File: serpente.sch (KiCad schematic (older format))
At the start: 24 parts, among them J1 USB_C_Receptacle_USB2.0, J2 Conn_Power, J3 Conn_GPIO, SW1 SW_RESET, U1 AT25SF081-XMHD-X, U2 MCP1700-3302E_SOT23, U3 ATSAMD21E1xA

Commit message: Rev 1
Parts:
- removed U1: AT25SF081-XMHD-X, Package_SO:TSSOP-8_4.4x3mm_P0.65mm, symbol Memory_Flash:AT25SF081-XMHD-X
- added R7, R8: 22R, Resistor_SMD:R_0603_1608Metric, symbol Device:R_Small
- added TP5: TP_USB_D-, TestPoint:TestPoint_Pad_D1.0mm, symbol Connector:TestPoint
- added TP6: TP_USB_D+, TestPoint:TestPoint_Pad_D1.0mm, symbol Connector:TestPoint
- added U1: GD25Q32CNIGR, Package_SON_Extra:USON-8_3x4mm_P0.8mm, symbol Memory_Flash_Extra:GD25Q32C
- C1, C2, C3, C4: footprint (none) -> Capacitor_SMD:C_0603_1608Metric
- D1, D2: footprint (none) -> Diode_SMD:D_SOD-323_HandSoldering
- D3: footprint (none) -> LED_SMD:LED_Cree-PLCC4_2x2mm_CW; symbol Device:LED_ARGB -> Device_Extra:LED_RBGA
- J1: footprint (none) -> Connector_USB_Extra:USB_C_Receptacle_GT-USB-7010
- J2: footprint (none) -> Connector_PinHeader_2.54mm:PinHeader_1x04_P2.54mm_Vertical
- J3: footprint (none) -> Connector_PinHeader_2.54mm:PinHeader_1x06_P2.54mm_Vertical
- R1: value TBD -> 360R; footprint (none) -> Resistor_SMD:R_0603_1608Metric
- R2, R3: value TBD -> 150R; footprint (none) -> Resistor_SMD:R_0603_1608Metric
- R4, R5, R6: footprint (none) -> Resistor_SMD:R_0603_1608Metric
- SW1: footprint (none) -> Button_Switch_SMD:SW_SPST_B3U-1000P
- TP1, TP2, TP3, TP4: footprint (none) -> TestPoint:TestPoint_Pad_D1.0mm
- U3: value ATSAMD21E1xA -> ATSAMD21E18A; footprint (none) -> Package_DFN_QFN:QFN-32-1EP_5x5mm_P0.5mm_EP3.6x3.6mm
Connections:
- wire segments 116 -> 120
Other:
- note added: "SERCOM 3 is always SPI FLASH\n\nPossible configs:\nSERCOM 0: SPI\n D0 - GPIO\n D1 - GPIO\n D2 - CS\n D3 - MISO\n D4 - SCK\n D5 - MOSI\n \nSERCOM 2: I2C\n D0 - SCL\n D1 - SDA\n D2 - GPIO\n D3 - GPIO\n D4 - GPIO\n D5 - GPIO\n\nSERCOM 0 or 2: UART\n D0 or D4 - RX\n D1 or D5 - TX\n D2 - GPIO\n D3 - GPIO\n\nSERCOM 0: UART, SERCOM 2: UART (2x UART)\n D0 - RX2\n D1 - TX2\n D2 - GPIO\n D3 - GPIO\n D4 - R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"
- note removed: "SERCOM 3 is always SPI FLASH\n\nPossible configs:\nSERCOM 0: SPI\n PA4 - MOSI\n PA5 - SCK\n PA6 - MISO\n PA7 - CS\n PA8 - GPIO\n PA9 - GPIO\n \nSERCOM 2: I2C\n PA4 - GPIO\n PA5 - GPIO\n PA6 - GPIO\n PA7 - GPIO\n PA8 - SDA\n PA9 - SCL\n\nSERCOM 0 or 2: UART\n PA4 or PA8 - TX\n PA6 - GPIO\n PA7 - GPIO\n PA5 or PA9 - RX\n\nSERCOM 0: UART, SERCOM 2: UART (2x UART)\n PA4 - TX0\n PA5 - RX0\n PA6 - GPIO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"
- note removed: "TODO:\nUpdate LED symbol\nUpdate FLASH symbol\nReplace PAx with GPIOx"
- moved on the sheet: J2, J3, R1, R2, R3, TP3, TP4

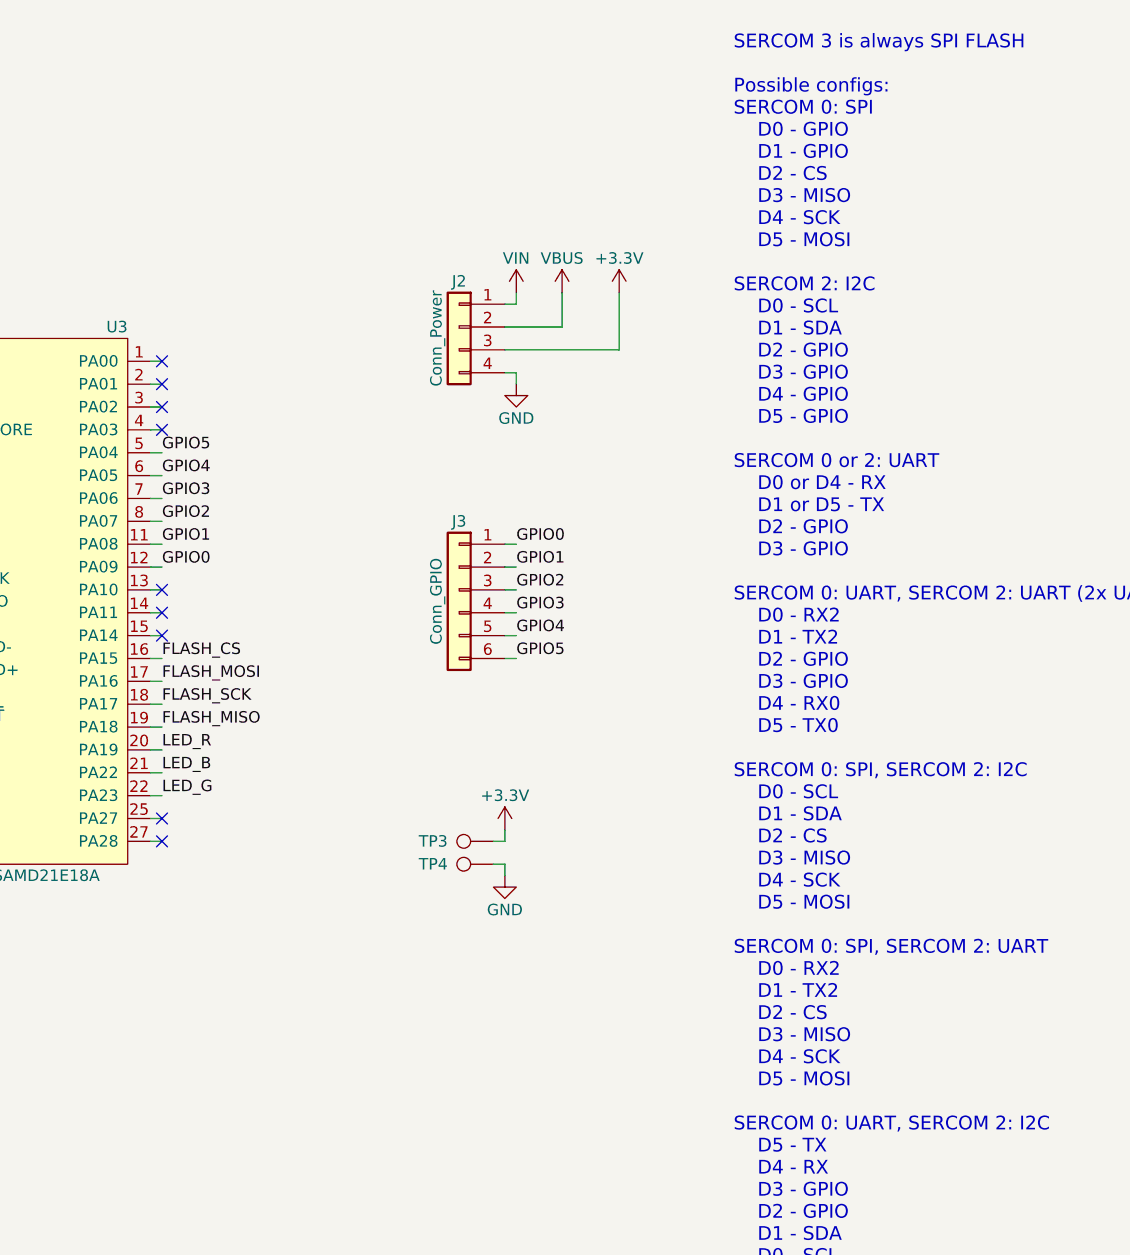
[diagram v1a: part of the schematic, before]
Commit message: Fix GPIO numbers, add BOM, update README
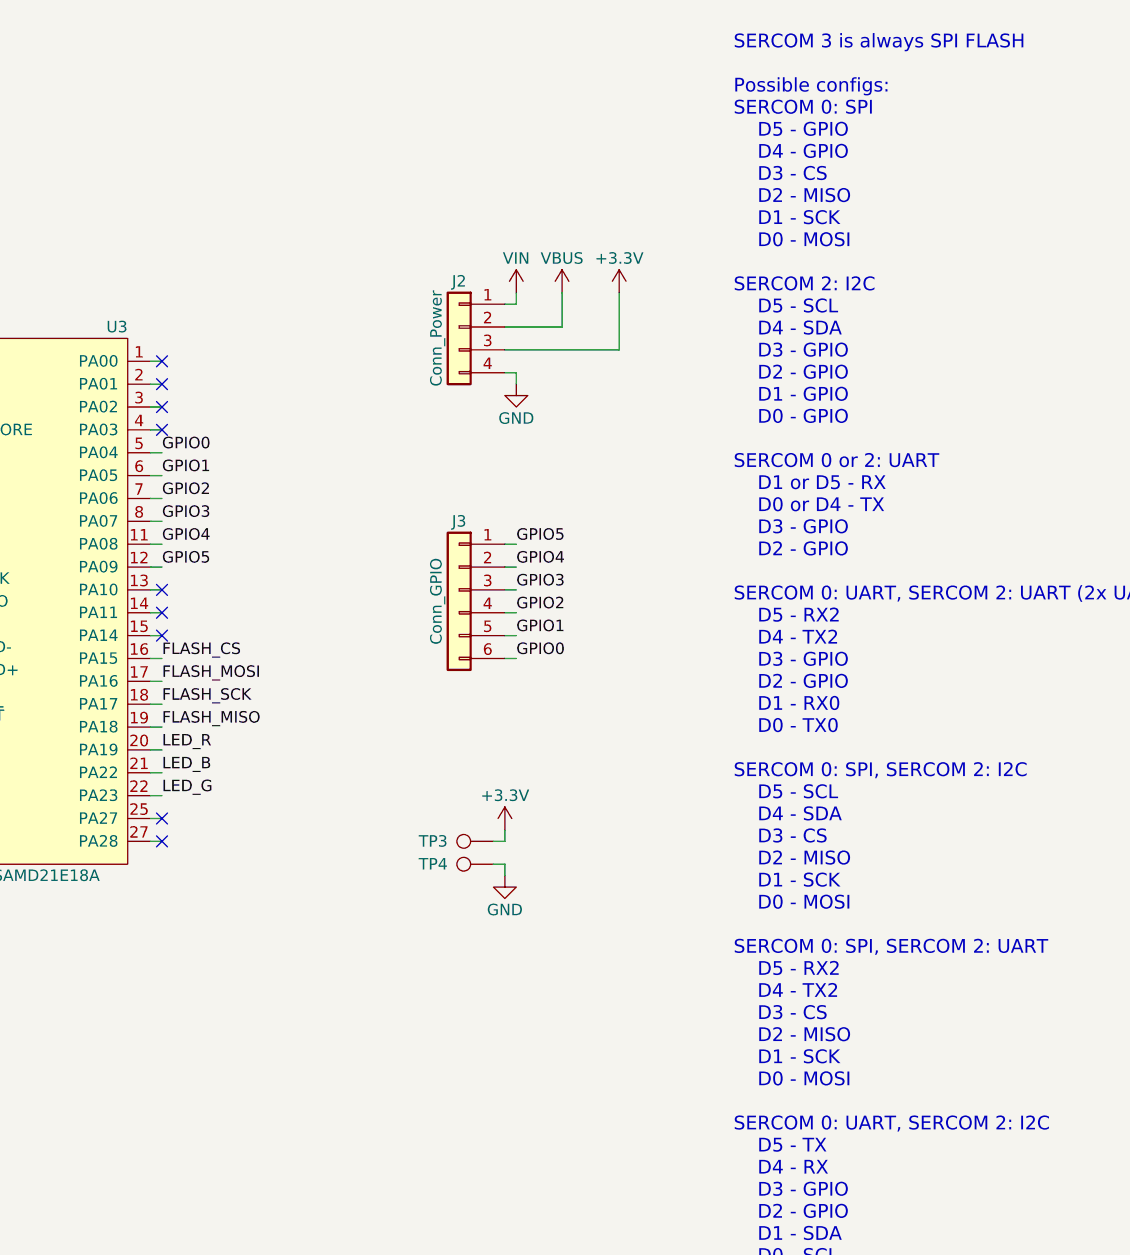
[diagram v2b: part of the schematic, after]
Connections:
- net GPIO0: now also J3.6 (Pin_6), U3.5 (PA04); no longer J3.1 (Pin_1), U3.12 (PA09)
- net GPIO1: now also J3.5 (Pin_5), U3.6 (PA05); no longer J3.2 (Pin_2), U3.11 (PA08)
- net GPIO2: now also J3.4 (Pin_4), U3.7 (PA06); no longer J3.3 (Pin_3), U3.8 (PA07)
- net GPIO3: now also J3.3 (Pin_3), U3.8 (PA07); no longer J3.4 (Pin_4), U3.7 (PA06)
- net GPIO4: now also J3.2 (Pin_2), U3.11 (PA08); no longer J3.5 (Pin_5), U3.6 (PA05)
- net GPIO5: now also J3.1 (Pin_1), U3.12 (PA09); no longer J3.6 (Pin_6), U3.5 (PA04)
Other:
- note added: "SERCOM 3 is always SPI FLASH\n\nPossible configs:\nSERCOM 0: SPI\n D5 - GPIO\n D4 - GPIO\n D3 - CS\n D2 - MISO\n D1 - SCK\n D0 - MOSI\n \nSERCOM 2: I2C\n D5 - SCL\n D4 - SDA\n D3 - GPIO\n D2 - GPIO\n D1 - GPIO\n D0 - GPIO\n\nSERCOM 0 or 2: UART\n D1 or D5 - RX\n D0 or D4 - TX\n D3 - GPIO\n D2 - GPIO\n\nSERCOM 0: UART, SERCOM 2: UART (2x UART)\n D5 - RX2\n D4 - TX2\n D3 - GPIO\n D2 - GPIO\n D1 - R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"
- note removed: "SERCOM 3 is always SPI FLASH\n\nPossible configs:\nSERCOM 0: SPI\n D0 - GPIO\n D1 - GPIO\n D2 - CS\n D3 - MISO\n D4 - SCK\n D5 - MOSI\n \nSERCOM 2: I2C\n D0 - SCL\n D1 - SDA\n D2 - GPIO\n D3 - GPIO\n D4 - GPIO\n D5 - GPIO\n\nSERCOM 0 or 2: UART\n D0 or D4 - RX\n D1 or D5 - TX\n D2 - GPIO\n D3 - GPIO\n\nSERCOM 0: UART, SERCOM 2: UART (2x UART)\n D0 - RX2\n D1 - TX2\n D2 - GPIO\n D3 - GPIO\n D4 - R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"
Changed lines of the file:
@@
 Text Label 6350 3900 0    50   ~ 0
 LED_B
+Text Label 7900 3400 0    50   ~ 0
+GPIO0
+Text Label 7900 3300 0    50   ~ 0
+GPIO1
+Text Label 7900 3200 0    50   ~ 0
+GPIO2
+Text Label 7900 3100 0    50   ~ 0
+GPIO3
+Text Label 7900 3000 0    50   ~ 0
+GPIO4
 Text Label 7900 2900 0    50   ~ 0
+GPIO5
+Text Label 6350 2500 0    50   ~ 0
 GPIO0
-Text Label 7900 3000 0    50   ~ 0
+Text Label 6350 2600 0    50   ~ 0
 GPIO1
-Text Label 7900 3100 0    50   ~ 0
+Text Label 6350 2700 0    50   ~ 0
 GPIO2
-Text Label 7900 3200 0    50   ~ 0
+Text Label 6350 2800 0    50   ~ 0
 GPIO3
-Text Label 7900 3300 0    50   ~ 0
+Text Label 6350 2900 0    50   ~ 0
 GPIO4
-Text Label 7900 3400 0    50   ~ 0
-GPIO5
 Text Label 6350 3000 0    50   ~ 0
-GPIO0
-Text Label 6350 2900 0    50   ~ 0
-GPIO1
-Text Label 6350 2800 0    50   ~ 0
-GPIO2
-Text Label 6350 2700 0    50   ~ 0
-GPIO3
-Text Label 6350 2600 0    50   ~ 0
-GPIO4
-Text Label 6350 2500 0    50   ~ 0
 GPIO5
 $Comp
@@
 FLASH_MISO
 Text Notes 8850 6250 0    60   ~ 0
-SERCOM 3 is always SPI FLASH\n\nPossible configs:\nSERCOM 0: SPI\n    D0 - GPIO\n    D1 - GPIO\n    D2 - CS\n    D3 - MISO\n    D4 - SCK\n    D5 - MOSI\n    \nSERCOM 2: I2C\n    D0 - SCL\n    D1 - SDA\n    D2 - GPIO\n    D3 - GPIO\n    D4 - GPIO\n    D5 - GPIO\n\nSERCOM 0 or 2: UART\n    D0 or D4 - RX\n    D1 or D5 - TX\n    D2 - GPIO\n    D3 - GPIO\n\nSERCOM 0: UART, SERCOM 2: UART (2x UART)\n    D0 - RX2\n    D1 - TX2\n    D2 - GPIO\n    D3 - GPIO\n    D4 - RX0\n    D5 - TX0\n\nSERCOM 0: SPI, SERCOM 2: I2C\n    D0 - SCL\n    D1 - SDA\n    D2 - CS\n    D3 - MISO\n    D4 - SCK\n    D5 - MOSI\n\nSERCOM 0: SPI, SERCOM 2: UART\n    D0 - RX2\n    D1 - TX2\n    D2 - CS\n    D3 - MISO\n    D4 - SCK\n    D5 - MOSI\n\nSERCOM 0: UART, SERCOM 2: I2C\n    D5 - TX\n    D4 - RX\n    D3 - GPIO\n    D2 - GPIO\n    D1 - SDA\n    D0 - SCL\n\nAll GPIOs are PWM-enabled!\n
+SERCOM 3 is always SPI FLASH\n\nPossible configs:\nSERCOM 0: SPI\n    D5 - GPIO\n    D4 - GPIO\n    D3 - CS\n    D2 - MISO\n    D1 - SCK\n    D0 - MOSI\n    \nSERCOM 2: I2C\n    D5 - SCL\n    D4 - SDA\n    D3 - GPIO\n    D2 - GPIO\n    D1 - GPIO\n    D0 - GPIO\n\nSERCOM 0 or 2: UART\n    D1 or D5 - RX\n    D0 or D4 - TX\n    D3 - GPIO\n    D2 - GPIO\n\nSERCOM 0: UART, SERCOM 2: UART (2x UART)\n    D5 - RX2\n    D4 - TX2\n    D3 - GPIO\n    D2 - GPIO\n    D1 - RX0\n    D0 - TX0\n\nSERCOM 0: SPI, SERCOM 2: I2C\n    D5 - SCL\n    D4 - SDA\n    D3 - CS\n    D2 - MISO\n    D1 - SCK\n    D0 - MOSI\n\nSERCOM 0: SPI, SERCOM 2: UART\n    D5 - RX2\n    D4 - TX2\n    D3 - CS\n    D2 - MISO\n    D1 - SCK\n    D0 - MOSI\n\nSERCOM 0: UART, SERCOM 2: I2C\n    D5 - TX\n    D4 - RX\n    D3 - GPIO\n    D2 - GPIO\n    D1 - SDA\n    D0 - SCL\n\nAll GPIOs are PWM-enabled!
 NoConn ~ 6350 2100
 NoConn ~ 6350 2200

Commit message: Final rev 2 release!
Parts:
- removed R7, R8: 22R, Resistor_SMD:R_0603_1608Metric, symbol Device:R_Small
- added TP7: TP_RESET, TestPoint:TestPoint_Pad_D1.0mm, symbol Connector:TestPoint
- D1, D2: LCSC (none) -> C114023
- D3: value LED_ARGB -> LED_RBAG; symbol Device_Extra:LED_RBGA -> Device_Extra:LED_RBAG; LCSC (none) -> C108793
- J1: LCSC (none) -> C319148
- J2: footprint Connector_PinHeader_2.54mm:PinHeader_1x04_P2.54mm_Vertical -> Connector_PinHeader_2.54mm_Extra:PinHeader_1x04_P2.54mm_Vertical_Castellated
- J3: footprint Connector_PinHeader_2.54mm:PinHeader_1x06_P2.54mm_Vertical -> Connector_PinHeader_2.54mm_Extra:PinHeader_1x06_P2.54mm_Vertical_Castellated
- SW1: footprint Button_Switch_SMD:SW_SPST_B3U-1000P -> Button_Switch_SMD:SW_SPST_B3U-1000P-B; LCSC (none) -> C128937
- U2: LCSC (none) -> C83932
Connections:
- net +3V3: now also D3.3 (A), J2.4 (Pin_4); no longer D3.4 (A), J2.3 (Pin_3)
- net GND: now also J2.3 (Pin_3); no longer J2.4 (Pin_4)
- net LED_B: now also U3.22 (PA23); no longer U3.21 (PA22)
- net LED_G: now also U3.20 (PA19); no longer U3.22 (PA23)
- net LED_R: now also U3.21 (PA22); no longer U3.20 (PA19)
- net USB_D+: now also U3.24 (USB_D+)
- net USB_D-: now also U3.23 (USB_D-)
- net ~RESET~: now reaches SW1.2 (B), U3.26 (~RESET~)
- net ~RESET~: now also TP7.1
- net at R2.1: now also D3.4 (GK); no longer D3.3 (GK)
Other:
- moved on the sheet: SW1, TP4, TP5, TP6
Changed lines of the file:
@@
-EESchema Schematic File Version 4
-LIBS:serpente-cache
-EELAYER 29 0
+EESchema Schematic File Version 5
+EELAYER 30 0
 EELAYER END
 $Descr A4 11693 8268
 encoding utf-8
 Sheet 1 1
-Title ""
+Title "Serpente"
 Date ""
-Rev ""
+Rev "2"
 Comp ""
 Comment1 ""
@@
 Comment3 ""
 Comment4 ""
+Comment5 ""
+Comment6 ""
+Comment7 ""
+Comment8 ""
+Comment9 ""
 $EndDescr
 Wire Wire Line
@@
 F 2 "Connector_USB_Extra:USB_C_Receptacle_GT-USB-7010" H 2300 1450 50  0001 C CNN
 F 3 "https://www.usb.org/sites/default/files/documents/usb_type-c.zip" H 2300 1450 50  0001 C CNN
+F 4 "C319148" H 2150 1450 50  0001 C CNN "LCSC"
 	1    2150 1450
 	1    0    0    -1
@@
 F 2 "Package_TO_SOT_SMD:SOT-23" H 2350 3625 50  0001 C CNN
 F 3 "http://ww1.microchip.com/downloads/en/DeviceDoc/20001826D.pdf" H 2350 3400 50  0001 C CNN
+F 4 "C83932" H 2350 3400 50  0001 C CNN "LCSC"
 	1    2350 3400
 	1    0    0    -1
@@
 F 2 "Diode_SMD:D_SOD-323_HandSoldering" V 1600 3250 50  0001 C CNN
 F 3 "~" V 1600 3250 50  0001 C CNN
+F 4 "C114023" H 1600 3250 50  0001 C CNN "LCSC"
 	1    1600 3250
 	0    1    -1   0
@@
 F 2 "Diode_SMD:D_SOD-323_HandSoldering" V 1800 3250 50  0001 C CNN
 F 3 "~" V 1800 3250 50  0001 C CNN
+F 4 "C114023" H 1800 3250 50  0001 C CNN "LCSC"
 	1    1800 3250
 	0    1    -1   0
@@
 L Switch:SW_SPST SW1
 U 1 1 5D580D9E
-P 5050 3650
-F 0 "SW1" H 5050 3550 50  0000 C CNN
-F 1 "SW_RESET" H 5050 3794 50  0001 C CNN
-F 2 "Button_Switch_SMD:SW_SPST_B3U-1000P" H 5050 3650 50  0001 C CNN
-F 3 "~" H 5050 3650 50  0001 C CNN
-	1    5050 3650
-	1    0    0    -1
-$EndComp
-Wire Wire Line
-	4850 3650 4800 3650
-Wire Wire Line
-	4800 3650 4800 3700
+P 4750 3650
+F 0 "SW1" H 4750 3550 50  0000 C CNN
+F 1 "SW_RESET" H 4750 3794 50  0001 C CNN
+F 2 "Button_Switch_SMD:SW_SPST_B3U-1000P-B" H 4750 3650 50  0001 C CNN
+F 3 "~" H 4750 3650 50  0001 C CNN
+F 4 "C128937" H 4750 3650 50  0001 C CNN "LCSC"
+	1    4750 3650
+	1    0    0    -1
+$EndComp
+Wire Wire Line
+	4550 3650 4500 3650
+Wire Wire Line
+	4500 3650 4500 3700
 $Comp
 L power:GND #PWR018
 U 1 1 5D581A2E
-P 4800 3700
-F 0 "#PWR018" H 4800 3450 50  0001 C CNN
-F 1 "GND" H 4805 3527 50  0000 C CNN
-F 2 "" H 4800 3700 50  0001 C CNN
-F 3 "" H 4800 3700 50  0001 C CNN
-	1    4800 3700
+P 4500 3700
+F 0 "#PWR018" H 4500 3450 50  0001 C CNN
+F 1 "GND" H 4505 3527 50  0000 C CNN
+F 2 "" H 4500 3700 50  0001 C CNN
+F 3 "" H 4500 3700 50  0001 C CNN
+	1    4500 3700
 	1    0    0    -1
 $EndComp
@@
 F 0 "J2" H 7650 2150 50  0000 C CNN
 F 1 "Conn_Power" V 7750 1900 50  0000 C CNN
-F 2 "Connector_PinHeader_2.54mm:PinHeader_1x04_P2.54mm_Vertical" H 7650 1950 50  0001 C CNN
+F 2 "Connector_PinHeader_2.54mm_Extra:PinHeader_1x04_P2.54mm_Vertical_Castellated" H 7650 1950 50  0001 C CNN
 F 3 "~" H 7650 1950 50  0001 C CNN
 	1    7650 1950
@@
 	8100 1950 8100 1800
 Wire Wire Line
-	7850 2150 7900 2150
-Wire Wire Line
-	7900 2150 7900 2200
+	7850 2050 7900 2050
 $Comp
 L power:GND #PWR025
 U 1 1 5D5EF97D
-P 7900 2200
-F 0 "#PWR025" H 7900 1950 50  0001 C CNN
-F 1 "GND" H 7900 2050 50  0000 C CNN
-F 2 "" H 7900 2200 50  0001 C CNN
-F 3 "" H 7900 2200 50  0001 C CNN
-	1    7900 2200
-	1    0    0    -1
+P 7900 2050
+F 0 "#PWR025" H 7900 1800 50  0001 C CNN
+F 1 "GND" V 7900 1850 50  0000 C CNN
+F 2 "" H 7900 2050 50  0001 C CNN
+F 3 "" H 7900 2050 50  0001 C CNN
+	1    7900 2050
+	0    -1   -1   0
 $EndComp
 $Comp
@@
 F 0 "J3" H 7650 3400 50  0000 C CNN
 F 1 "Conn_GPIO" V 7750 3050 50  0000 C CNN
-F 2 "Connector_PinHeader_2.54mm:PinHeader_1x06_P2.54mm_Vertical" H 7650 3100 50  0001 C CNN
+F 2 "Connector_PinHeader_2.54mm_Extra:PinHeader_1x06_P2.54mm_Vertical_Castellated" H 7650 3100 50  0001 C CNN
 F 3 "~" H 7650 3100 50  0001 C CNN
 	1    7650 3100
@@
 L Connector:TestPoint TP4
 U 1 1 5D60E018
-P 7800 4300
-F 0 "TP4" V 7800 4500 50  0000 L CNN
-F 1 "TP_GND" V 7904 4372 50  0001 C CNN
-F 2 "TestPoint:TestPoint_Pad_D1.0mm" H 8000 4300 50  0001 C CNN
-F 3 "~" H 8000 4300 50  0001 C CNN
-	1    7800 4300
+P 7800 4400
+F 0 "TP4" V 7800 4600 50  0000 L CNN
+F 1 "TP_GND" V 7904 4472 50  0001 C CNN
+F 2 "TestPoint:TestPoint_Pad_D1.0mm" H 8000 4400 50  0001 C CNN
+F 3 "~" H 8000 4400 50  0001 C CNN
+	1    7800 4400
 	0    -1   -1   0
 $EndComp
@@
 	7850 4200 7850 4150
 Wire Wire Line
-	7800 4300 7850 4300
-Wire Wire Line
-	7850 4300 7850 4350
+	7800 4400 7850 4400
+Wire Wire Line
+	7850 4400 7850 4450
 $Comp
 L power:GND #PWR023
 U 1 1 5D6136B1
-P 7850 4350
-F 0 "#PWR023" H 7850 4100 50  0001 C CNN
-F 1 "GND" H 7850 4200 50  0000 C CNN
-F 2 "" H 7850 4350 50  0001 C CNN
-F 3 "" H 7850 4350 50  0001 C CNN
-	1    7850 4350
+P 7850 4450
+F 0 "#PWR023" H 7850 4200 50  0001 C CNN
+F 1 "GND" H 7850 4300 50  0000 C CNN
+F 2 "" H 7850 4450 50  0001 C CNN
+F 3 "" H 7850 4450 50  0001 C CNN
+	1    7850 4450
 	1    0    0    -1
 $EndComp
@@
 Text Label 2650 4800 0    50   ~ 0
 FLASH_MISO
+Text Label 6350 3900 0    50   ~ 0
+LED_R
 Text Label 6350 3800 0    50   ~ 0
-LED_R
+LED_G
 Text Label 6350 4000 0    50   ~ 0
-LED_G
-Text Label 6350 3900 0    50   ~ 0
 LED_B
 Text Label 7900 3400 0    50   ~ 0
@@
 	0    -1   -1   0
 $EndComp
-Text Label 4750 3350 2    50   ~ 0
+Text Label 5250 3350 2    50   ~ 0
 USB_D-
-Text Label 4750 3450 2    50   ~ 0
+Text Label 5250 3450 2    50   ~ 0
 USB_D+
 NoConn ~ 6350 4200
@@
 NoConn ~ 6350 3200
 NoConn ~ 6350 3300
-Wire Wire Line
-	5250 3650 5300 3650
 $Comp
 L power:+5V #PWR0101
@@
 $EndComp
 $Comp
-L Device_Extra:LED_RBGA D3
+L Device_Extra:LED_RBAG D3
 U 1 1 5D63A1CD
 P 2500 6000
 F 0 "D3" H 2500 6400 50  0000 C CNN
-F 1 "LED_ARGB" H 2500 5650 50  0000 C CNN
+F 1 "LED_RBAG" H 2500 5650 50  0000 C CNN
 F 2 "LED_SMD:LED_Cree-PLCC4_2x2mm_CW" H 2500 5950 50  0001 C CNN
 F 3 "~" H 2500 5950 50  0001 C CNN
+F 4 "C108793" H 2500 6000 50  0001 C CNN "LCSC"
 	1    2500 6000
 	1    0    0    -1
@@
 $EndComp
 $Comp
-L Device:R_Small R7
-U 1 1 5D663658
-P 5000 3350
-F 0 "R7" V 4950 3250 50  0000 R CNN
-F 1 "22R" V 4950 3450 50  0000 L CNN
-F 2 "Resistor_SMD:R_0603_1608Metric" H 5000 3350 50  0001 C CNN
-F 3 "~" H 5000 3350 50  0001 C CNN
-	1    5000 3350
-	0    1    1    0
-$EndComp
-$Comp
-L Device:R_Small R8
-U 1 1 5D6642A1
-P 5000 3450
-F 0 "R8" V 4950 3350 50  0000 R CNN
-F 1 "22R" V 4950 3550 50  0000 L CNN
-F 2 "Resistor_SMD:R_0603_1608Metric" H 5000 3450 50  0001 C CNN
-F 3 "~" H 5000 3450 50  0001 C CNN
-	1    5000 3450
-	0    1    1    0
-$EndComp
-Wire Wire Line
-	5100 3450 5300 3450
-Wire Wire Line
-	5100 3350 5300 3350
-$Comp
 L Connector:TestPoint TP5
 U 1 1 5D6C95EC
-P 4450 3350
-F 0 "TP5" V 4450 3550 50  0000 L CNN
-F 1 "TP_USB_D-" V 4554 3422 50  0001 C CNN
-F 2 "TestPoint:TestPoint_Pad_D1.0mm" H 4650 3350 50  0001 C CNN
-F 3 "~" H 4650 3350 50  0001 C CNN
-	1    4450 3350
+P 4950 3350
+F 0 "TP5" V 4950 3550 50  0000 L CNN
+F 1 "TP_USB_D-" V 5054 3422 50  0001 C CNN
+F 2 "TestPoint:TestPoint_Pad_D1.0mm" H 5150 3350 50  0001 C CNN
+F 3 "~" H 5150 3350 50  0001 C CNN
+	1    4950 3350
 	0    -1   -1   0
 $EndComp
@@
 L Connector:TestPoint TP6
 U 1 1 5D6CB8FB
-P 4450 3450
-F 0 "TP6" V 4450 3650 50  0000 L CNN
-F 1 "TP_USB_D+" V 4554 3522 50  0001 C CNN
-F 2 "TestPoint:TestPoint_Pad_D1.0mm" H 4650 3450 50  0001 C CNN
-F 3 "~" H 4650 3450 50  0001 C CNN
-	1    4450 3450
+P 4950 3450
+F 0 "TP6" V 4950 3650 50  0000 L CNN
+F 1 "TP_USB_D+" V 5054 3522 50  0001 C CNN
+F 2 "TestPoint:TestPoint_Pad_D1.0mm" H 5150 3450 50  0001 C CNN
+F 3 "~" H 5150 3450 50  0001 C CNN
+	1    4950 3450
 	0    -1   -1   0
 $EndComp
-Wire Wire Line
-	4450 3350 4900 3350
-Wire Wire Line
-	4450 3450 4900 3450
 $Comp
 L power:+3.3V #PWR0108
@@
 $EndComp
 Wire Wire Line
-	7850 2050 8350 2050
-Wire Wire Line
-	8350 2050 8350 1800
+	7850 2150 8350 2150
+Wire Wire Line
+	8350 2150 8350 1800
+$Comp
+L Connector:TestPoint TP7
+U 1 1 5D8ED0C1
+P 7800 4300
+F 0 "TP7" V 7800 4500 50  0000 L CNN
+F 1 "TP_RESET" V 7904 4372 50  0001 C CNN
+F 2 "TestPoint:TestPoint_Pad_D1.0mm" H 8000 4300 50  0001 C CNN
+F 3 "~" H 8000 4300 50  0001 C CNN
+	1    7800 4300
+	0    -1   -1   0
+$EndComp
+Text Label 5250 3650 2    50   ~ 0
+~RESET~
+Text Label 7850 4300 0    50   ~ 0
+~RESET~
+Wire Wire Line
+	7800 4300 7850 4300
+Wire Wire Line
+	4950 3650 5300 3650
+Wire Wire Line
+	4950 3450 5300 3450
+Wire Wire Line
+	4950 3350 5300 3350
 $EndSCHEMATC
